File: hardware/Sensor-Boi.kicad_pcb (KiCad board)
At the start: 2 copper layers, 1 part, among them U1 ESP32-S3-WROOM-1

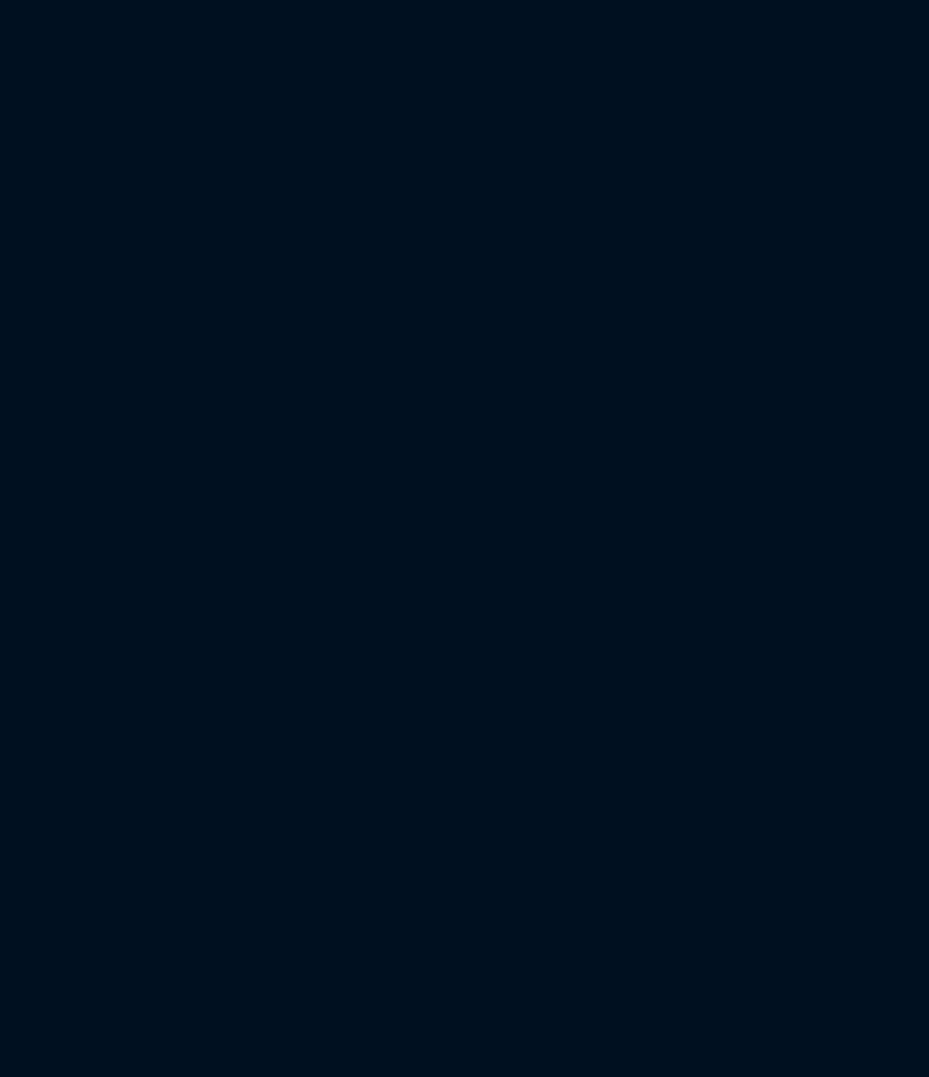
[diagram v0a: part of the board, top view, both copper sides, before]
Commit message: add a majority of symbols to schematic
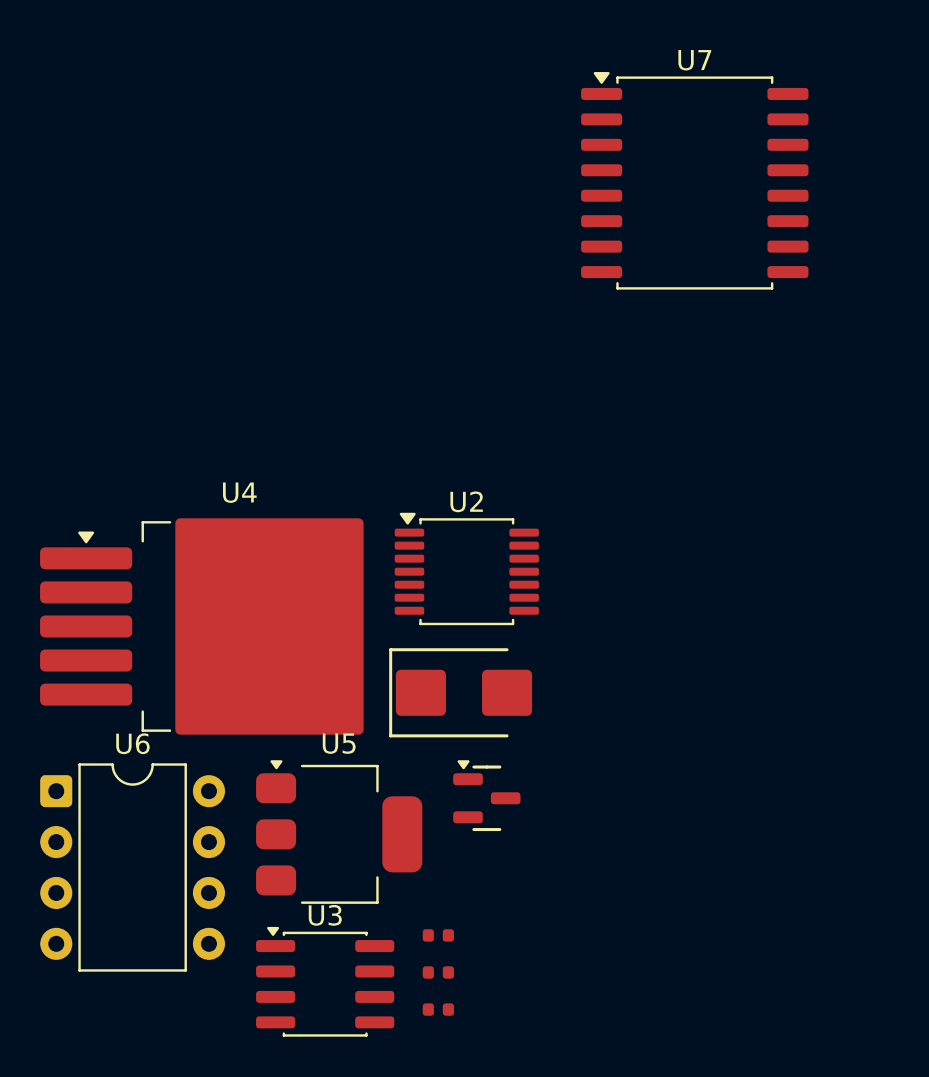
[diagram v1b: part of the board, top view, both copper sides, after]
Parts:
- added D1: BZX84C5V1, PCM_JLCPCB:D_SOT-23, F.Cu at (74.8, 89.5)
- added D2: SMBJ15A, PCM_JLCPCB:D_SMB, F.Cu at (73.7, 84.2)
- added R1: 100kΩ, PCM_JLCPCB:R_0402, F.Cu at (72.4, 96.3)
- added R2: 470Ω, PCM_JLCPCB:R_0402, F.Cu at (72.4, 98.2)
- added R3: 120Ω, PCM_JLCPCB:R_0402, F.Cu at (72.4, 100.0)
- added U2: MAX31856, Package_SO:TSSOP-14_4.4x5mm_P0.65mm, F.Cu at (73.8, 78.2)
- added U3: SN65HVD230, Package_SO:SOIC-8_3.9x4.9mm_P1.27mm, F.Cu at (66.8, 98.8)
- added U4: LM2596S-5, Package_TO_SOT_SMD:TO-263-5_TabPin3, F.Cu at (62.5, 80.9)
- added U5: AMS1117-3.3, Package_TO_SOT_SMD:SOT-223-3_TabPin2, F.Cu at (67.5, 91.3)
- added U6: 6N137, Package_DIP:DIP-8_W7.62mm, F.Cu at (53.3, 89.1)
- added U7: ISO7741DWR, Package_SO:SOIC-16W_7.5x10.3mm_P1.27mm, F.Cu at (85.2, 58.8)
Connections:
- net Net-(U1-GND-Pad1) renamed GND
- U1 pad 2: unconnected-(U1-3V3-Pad2) -> /3V3

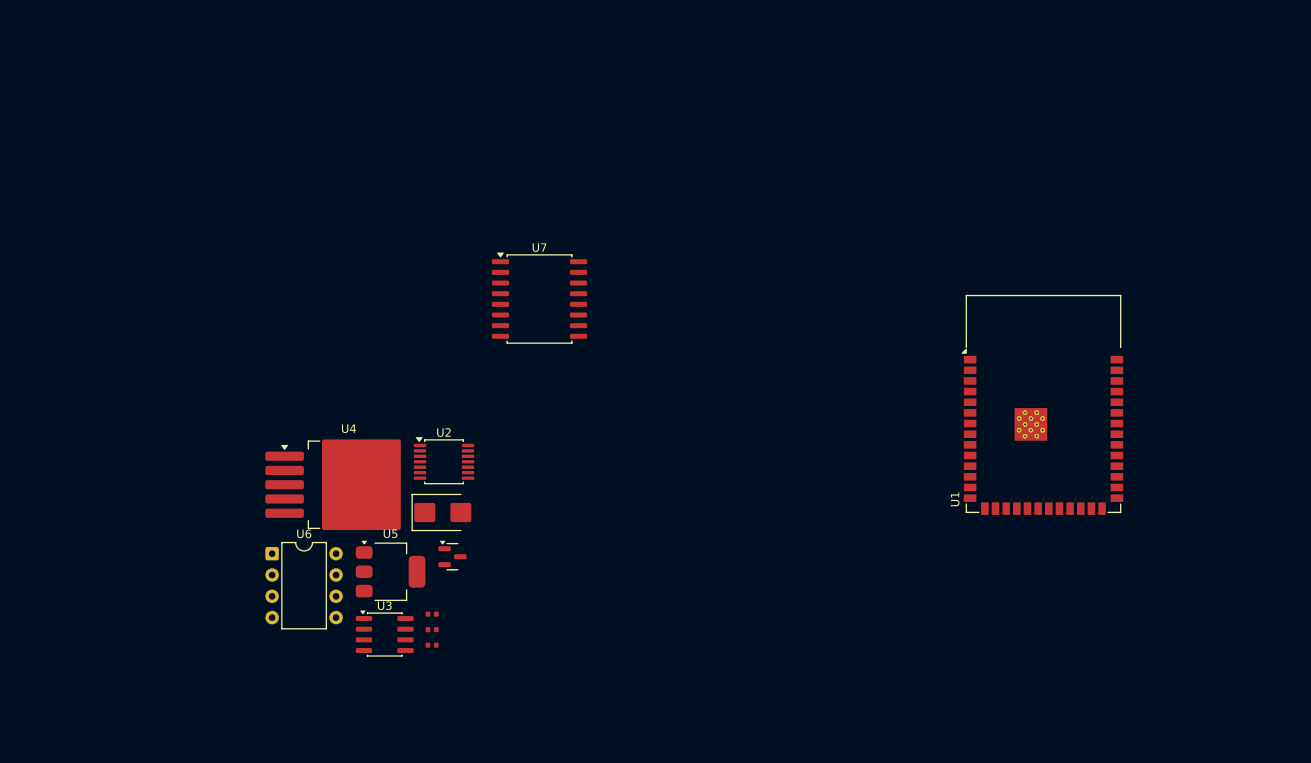
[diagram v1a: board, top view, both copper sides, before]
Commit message: add outline to pcb
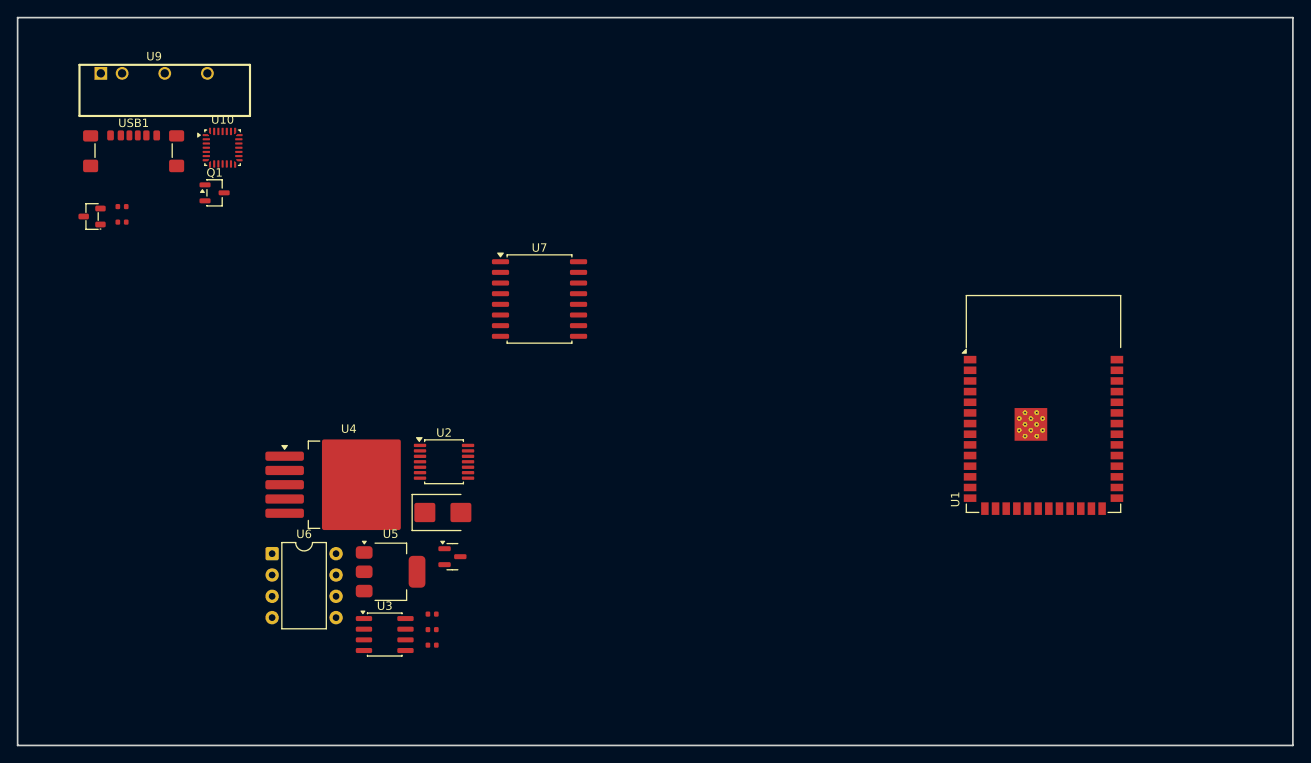
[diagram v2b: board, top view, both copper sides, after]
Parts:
- added C1: 100nF, PCM_JLCPCB:C_0402, F.Cu at (35.4, 47.8)
- added Q1: 2N7002, Package_TO_SOT_SMD:SOT-23-3, F.Cu at (46.5, 46.1)
- added R4: 5.1kΩ, PCM_JLCPCB:R_0402, F.Cu at (35.4, 49.6)
- added U10: CP2102N-A02-GQFN24R, Package_DFN_QFN:QFN-28_4x4mm_P0.5mm, F.Cu at (47.4, 40.8)
- added U8: LTC4412ES6_TRPBF, PCM_JLCPCB:SOT-23-3_L2.9-W1.3-P0.95-LS2.4-BR, F.Cu at (31.9, 49.0)
- added U9: B0505LS-1WR3_C7465180, JLCImport:B0505LS-1WR3_C7465180, F.Cu at (39.3, 31.9)
- added USB1: USB4085-GF-A_C7095263, Connector_USB:USB_C_Receptacle_GCT_USB4135-GF-A_6P_TopMnt_Horizontal, F.Cu at (36.8, 42.3)
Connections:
- R3 pad 1: unconnected-(R3-Pad1) -> /CAN_H
- R3 pad 2: unconnected-(R3-Pad2) -> /CAN_L
- U2 pad 10: unconnected-(U2-SCK-Pad10) -> /TEMP_SCK
- U2 pad 11: unconnected-(U2-SDO-Pad11) -> /TEMP_SDO
- U2 pad 12: unconnected-(U2-SDI-Pad12) -> /TEMP_SDI
- U2 pad 3: unconnected-(U2-T--Pad3) -> /CHT_-
- U2 pad 4: unconnected-(U2-T+-Pad4) -> /CHT_+
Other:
- board outline added: 152 x 86.8 mm

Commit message: add power electronics and connections
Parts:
- added C2: 100nF, PCM_JLCPCB:C_0402, F.Cu at (98.4, 80.2)
- added C3: 100nF, PCM_JLCPCB:C_0402, F.Cu at (98.4, 82.0)
- added C4: 100nF, PCM_JLCPCB:C_0402, F.Cu at (98.4, 83.9)
- added D3: BZX84C3V3, PCM_JLCPCB:D_SOT-23, F.Cu at (102.3, 81.7)
- added D4: BZX84C3V3, PCM_JLCPCB:D_SOT-23, F.Cu at (102.3, 86.3)
- added R5: 100Ω, PCM_JLCPCB:R_0402, F.Cu at (98.4, 85.7)
- added R6: 10kΩ, PCM_JLCPCB:R_0402, F.Cu at (98.4, 87.6)
- added R7: 15kΩ, PCM_JLCPCB:R_0402, F.Cu at (98.4, 89.4)
- added R8: 10kΩ, PCM_JLCPCB:R_0402, F.Cu at (98.4, 91.3)
- added R9: 180Ω, PCM_JLCPCB:R_0402, F.Cu at (98.4, 93.1)
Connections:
- U1 pad 10: unconnected-(U1-IO17-Pad10) -> /CAN_RX
- U1 pad 11: unconnected-(U1-IO18-Pad11) -> /CAN_TX
- U1 pad 13: unconnected-(U1-USB_D--Pad13) -> /USB_D-
- U1 pad 14: unconnected-(U1-USB_D+-Pad14) -> /USB_D+
- U1 pad 15: unconnected-(U1-IO3-Pad15) -> /PB_Bat_MCU
- U1 pad 38: unconnected-(U1-IO2-Pad38) -> /OIL_MCU
- U1 pad 39: unconnected-(U1-IO1-Pad39) -> /MAP_Signal_MCU
- U1 pad 4: unconnected-(U1-IO4-Pad4) -> /RPM_MCU
- U1 pad 5: unconnected-(U1-IO5-Pad5) -> /Wheel_Speed_MCU
- U1 pad 6: unconnected-(U1-IO6-Pad6) -> /Lambda_MCU
- U2 pad 1: unconnected-(U2-AGND-Pad1) -> GND2
- U2 pad 14: GND -> GND2
- U2 pad 5: unconnected-(U2-AVDD-Pad5) -> /3V3_Isolated
- U2 pad 8: unconnected-(U2-DVDD-Pad8) -> /3V3_Isolated
- U3 pad 1: unconnected-(U3-D-Pad1) -> /CAN_TX
- U3 pad 3: /5V -> /3V3
- U3 pad 4: unconnected-(U3-R-Pad4) -> /CAN_RX
- U7 pad 1: unconnected-(U7-VCC1-Pad1) -> /3V3_Isolated
- U7 pad 12: unconnected-(U7-OUTC-Pad12) -> /TEMP_SDI_MCU
- U7 pad 13: unconnected-(U7-OUTB-Pad13) -> /TEMP_SDO_MCU
- U7 pad 14: unconnected-(U7-OUTA-Pad14) -> /TEMP_SCK_MCU
- U7 pad 15: unconnected-(U7-GND2-Pad15) -> GND
- U7 pad 16: unconnected-(U7-VCC2-Pad16) -> /3V3
- U7 pad 2: unconnected-(U7-GND1-Pad2) -> GND2
- U7 pad 3: unconnected-(U7-INA-Pad3) -> /TEMP_SCK
- U7 pad 4: unconnected-(U7-INB-Pad4) -> /TEMP_SDO
- U7 pad 5: unconnected-(U7-INC-Pad5) -> /TEMP_SDI
- U9 pad 1: unconnected-(U9-VIN-Pad1) -> /3V3
- U9 pad 4: unconnected-(U9-0V-Pad4) -> GND2
- U9 pad 6: unconnected-(U9-+Vo-Pad6) -> /3V3_Isolated
